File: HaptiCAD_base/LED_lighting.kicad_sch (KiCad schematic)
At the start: 35 parts, among them U201 SN74LV1T34DBV

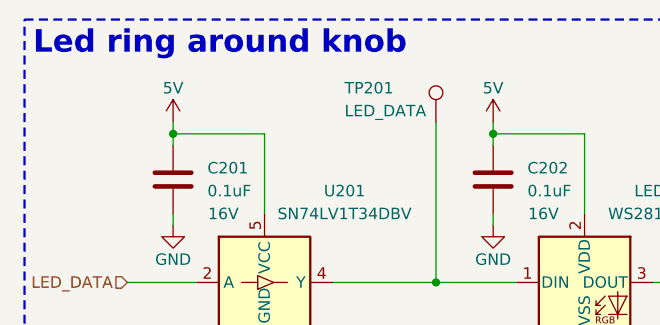
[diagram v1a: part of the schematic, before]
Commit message: updated base schematic and PCB
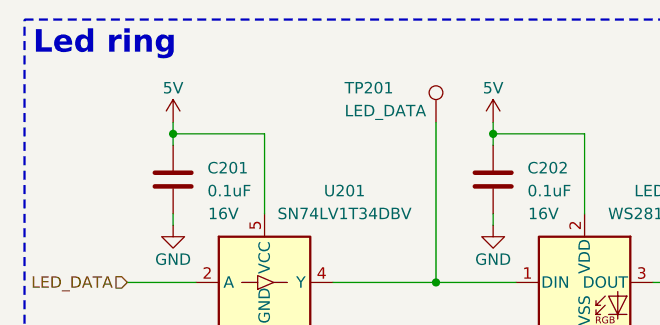
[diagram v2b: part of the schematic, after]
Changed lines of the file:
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@@
 		(company "Author: Emiel V")
 	)
-	(text_box "Led ring around knob"
+	(text_box "Led ring"
 		(exclude_from_sim no)
 		(at 16.51 52.07 0)

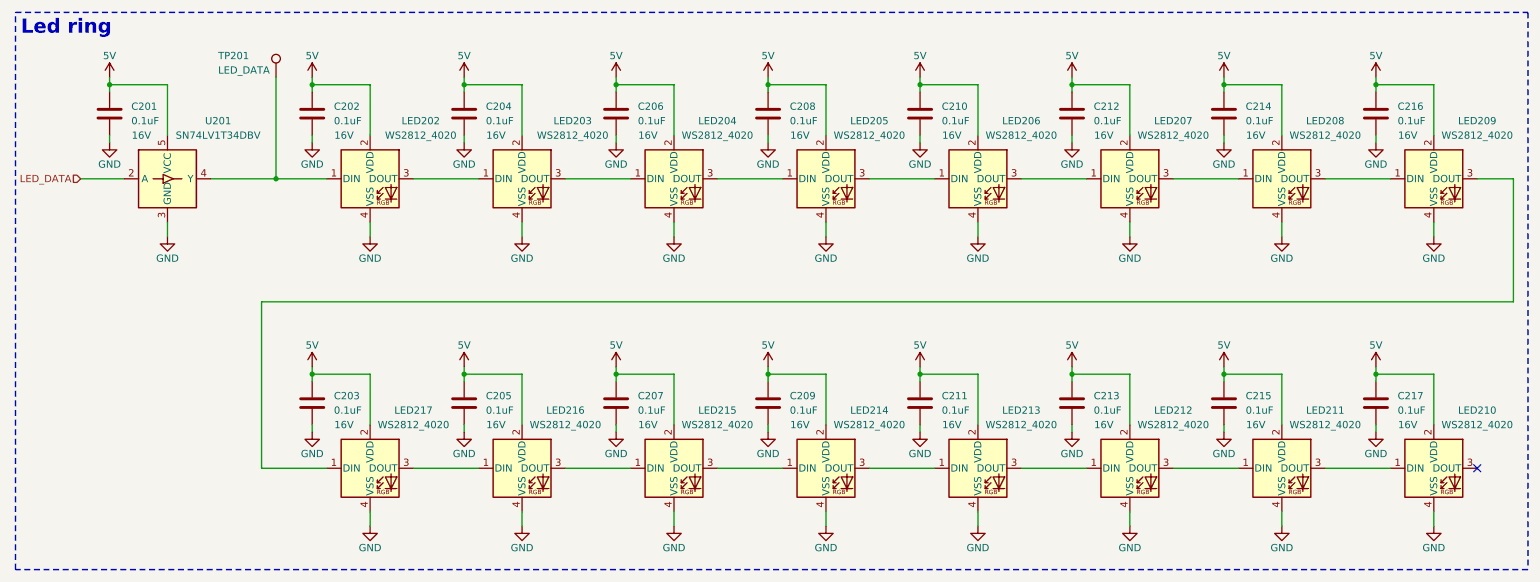
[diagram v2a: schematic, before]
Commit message: Finished schematic of the base board
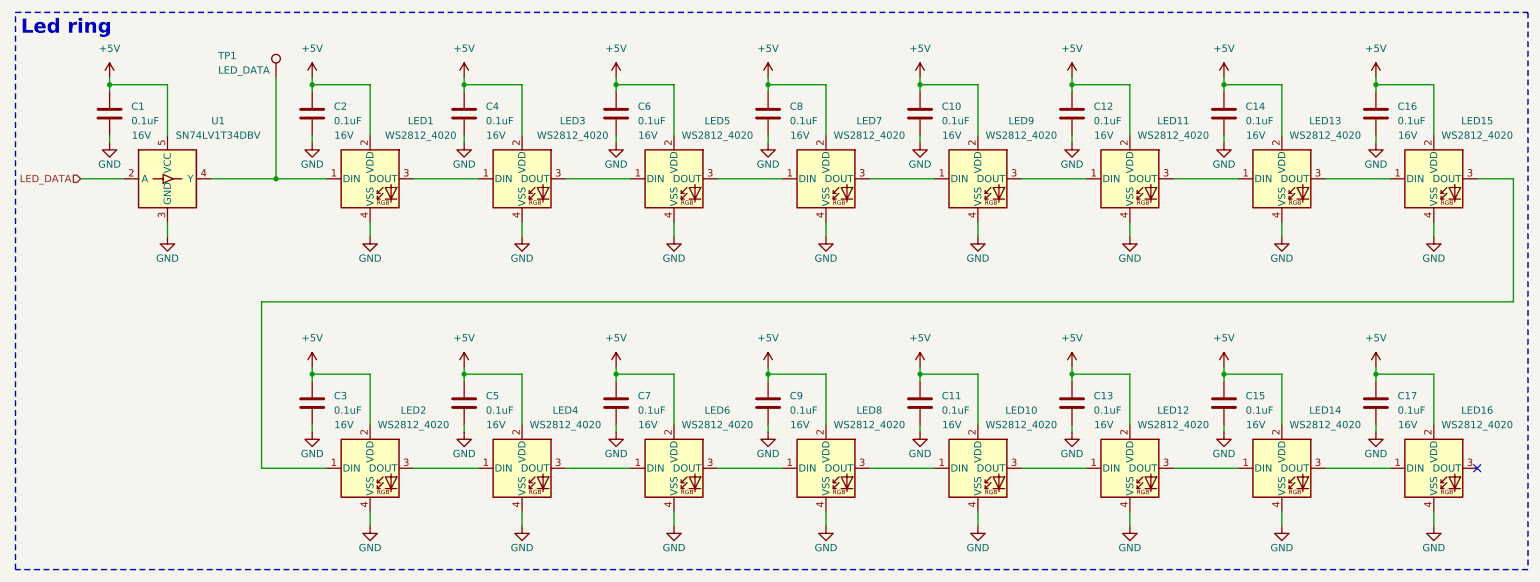
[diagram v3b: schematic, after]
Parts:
- renumbered C201 to C1, C210 to C10, C211 to C11, C212 to C12, C213 to C13, C214 to C14, C215 to C15, C216 to C16, C217 to C17, C202 to C2, C203 to C3, C204 to C4, C205 to C5, C206 to C6, C207 to C7, C208 to C8, C209 to C9, LED202 to LED1, LED213 to LED10, LED207 to LED11, LED212 to LED12, LED208 to LED13, LED211 to LED14, LED209 to LED15, LED210 to LED16, LED217 to LED2, LED203 to LED3, LED216 to LED4, LED204 to LED5, LED215 to LED6, LED205 to LED7, LED214 to LED8, LED206 to LED9, TP201 to TP1, U201 to U1
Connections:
- net 5V renamed +5V

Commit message: Finished the layout for the base and motor mount
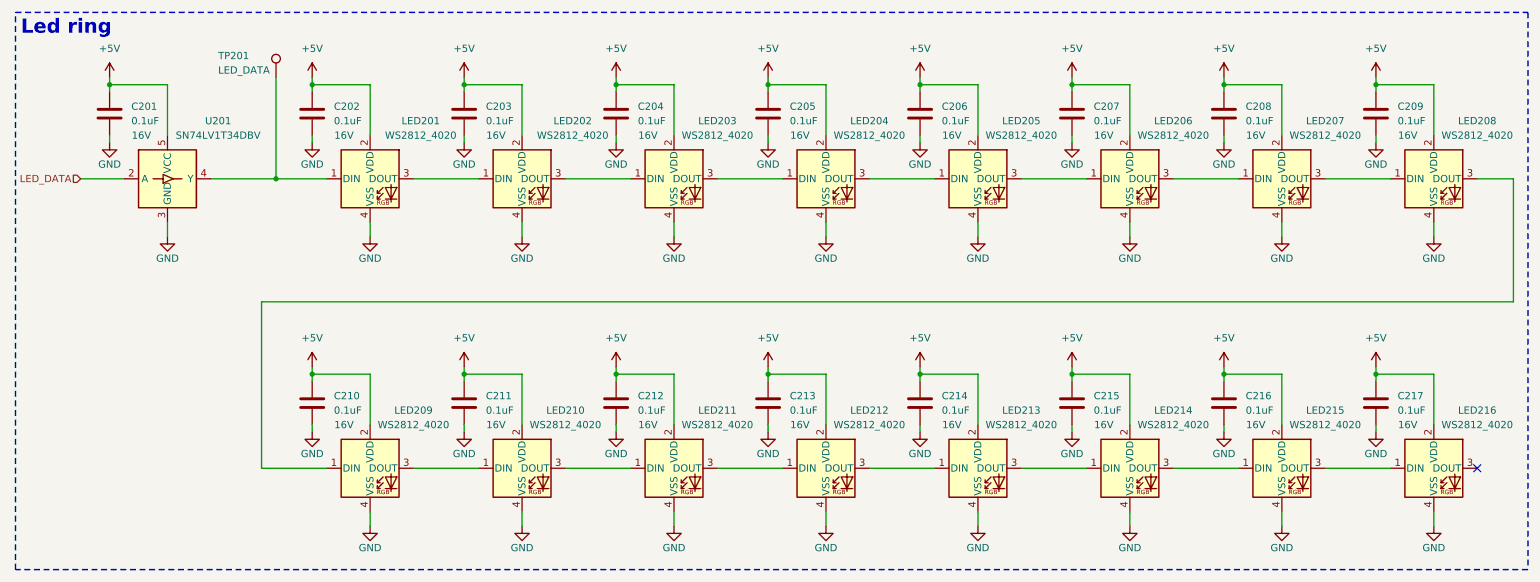
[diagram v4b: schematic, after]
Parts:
- renumbered C1 to C201, C2 to C202, C4 to C203, C6 to C204, C8 to C205, C10 to C206, C12 to C207, C14 to C208, C16 to C209, C3 to C210, C5 to C211, C7 to C212, C9 to C213, C11 to C214, C13 to C215, C15 to C216, C17 to C217, LED1 to LED201, LED3 to LED202, LED5 to LED203, LED7 to LED204, LED9 to LED205, LED11 to LED206, LED13 to LED207, LED15 to LED208, LED2 to LED209, LED4 to LED210, LED6 to LED211, LED8 to LED212, LED10 to LED213, LED12 to LED214, LED14 to LED215, LED16 to LED216, TP1 to TP201, U1 to U201
